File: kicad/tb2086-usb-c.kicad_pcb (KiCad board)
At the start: 2 copper layers, 29.3 x 19.5 mm, 17 parts, among them J1 Conn_01x04, U1 SRV05-4

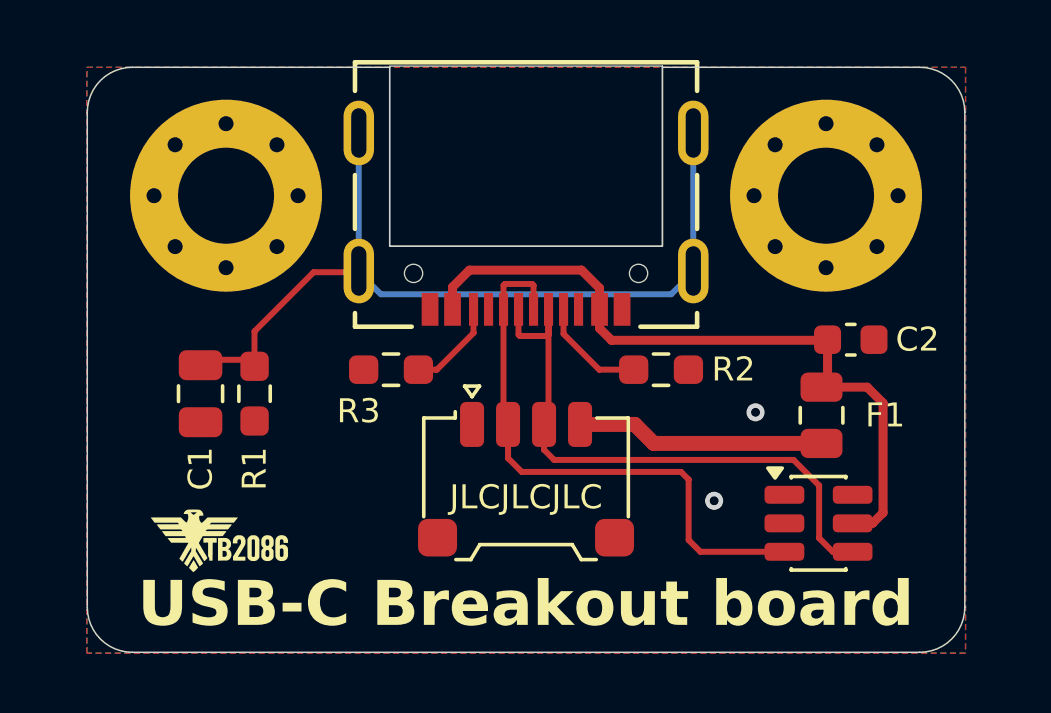
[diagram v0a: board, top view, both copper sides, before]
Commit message: replaced ESD protection
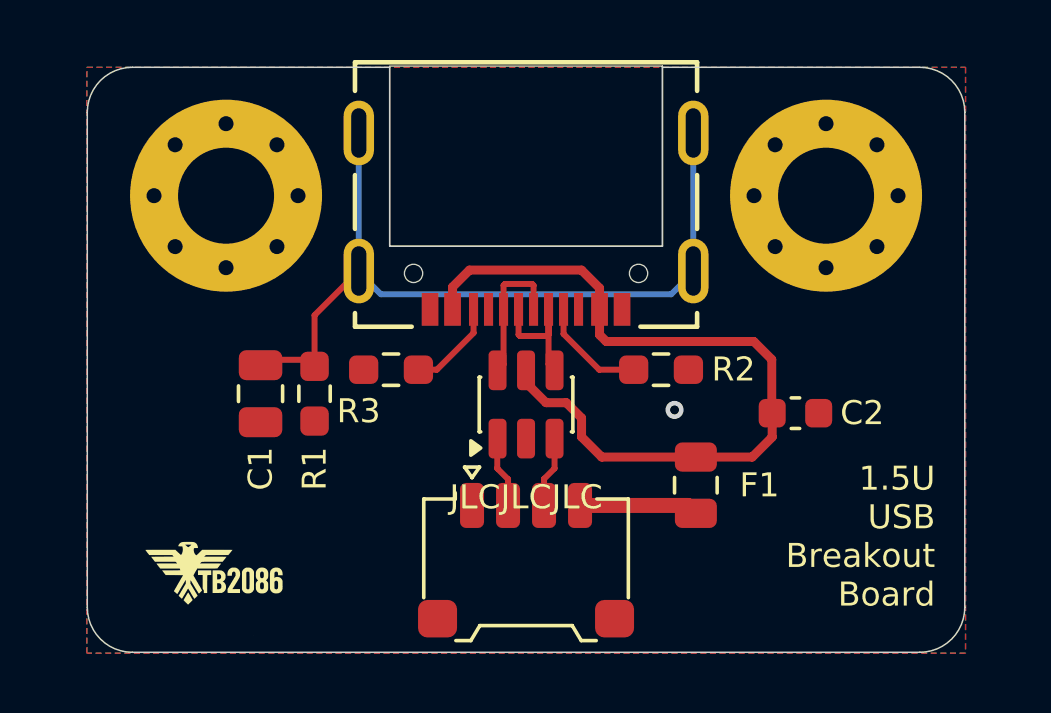
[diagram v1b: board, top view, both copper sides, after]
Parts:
- U1: value SRV05-4 -> USBLC6-2SC6
- moved U1 10.5 mm to (116.5, 69.7), turned to 90 degrees
- moved F1 4.79 mm to (122.2, 72.4)
- moved C2 3.07 mm to (125.5, 70.0)
- moved J1 2.70 mm to (116.5, 75.0)
- moved C1 2.00 mm to (107.7, 69.4)
- moved R1 2.00 mm to (109.5, 69.4)
- moved G*** 1.09 mm to (106.2, 75.3)
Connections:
- U1 pad 1: unconnected-(U1-IO1-Pad1) -> DATA+
- U1 pad 3: DATA+ -> DATA-
- U1 pad 4: DATA- -> USB_DATA-
- U1 pad 6: unconnected-(U1-IO4-Pad6) -> USB_DATA+
- USB1 pad A6: DATA+ -> USB_DATA+
- USB1 pad A7: DATA- -> USB_DATA-
- USB1 pad B6: DATA+ -> USB_DATA+
- USB1 pad B7: DATA- -> USB_DATA-
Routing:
- net DATA-: track 19.9 -> 2.37 mm
- net DATA+: track 19.3 -> 2.38 mm
- net USB_DATA-: track 0.00 -> 4.76 mm
- net USB_DATA+: track 0.00 -> 4.76 mm
- net +5V: track 8.31 -> 3.97 mm
- net VBUS: track 23.5 -> 26.6 mm
- net Net-(USB1-Shield): track 28.0 -> 26.5 mm
- net GND: vias 2 -> 1
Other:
- board text added: "1.5U USB Breakout Board"
- board text added: "2025.11.23"
- board text removed: "2025.11.22"
